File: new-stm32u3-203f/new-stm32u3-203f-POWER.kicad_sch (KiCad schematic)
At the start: 15 parts, among them U4 LD39050PU33R, U5 TLV62569DBVR

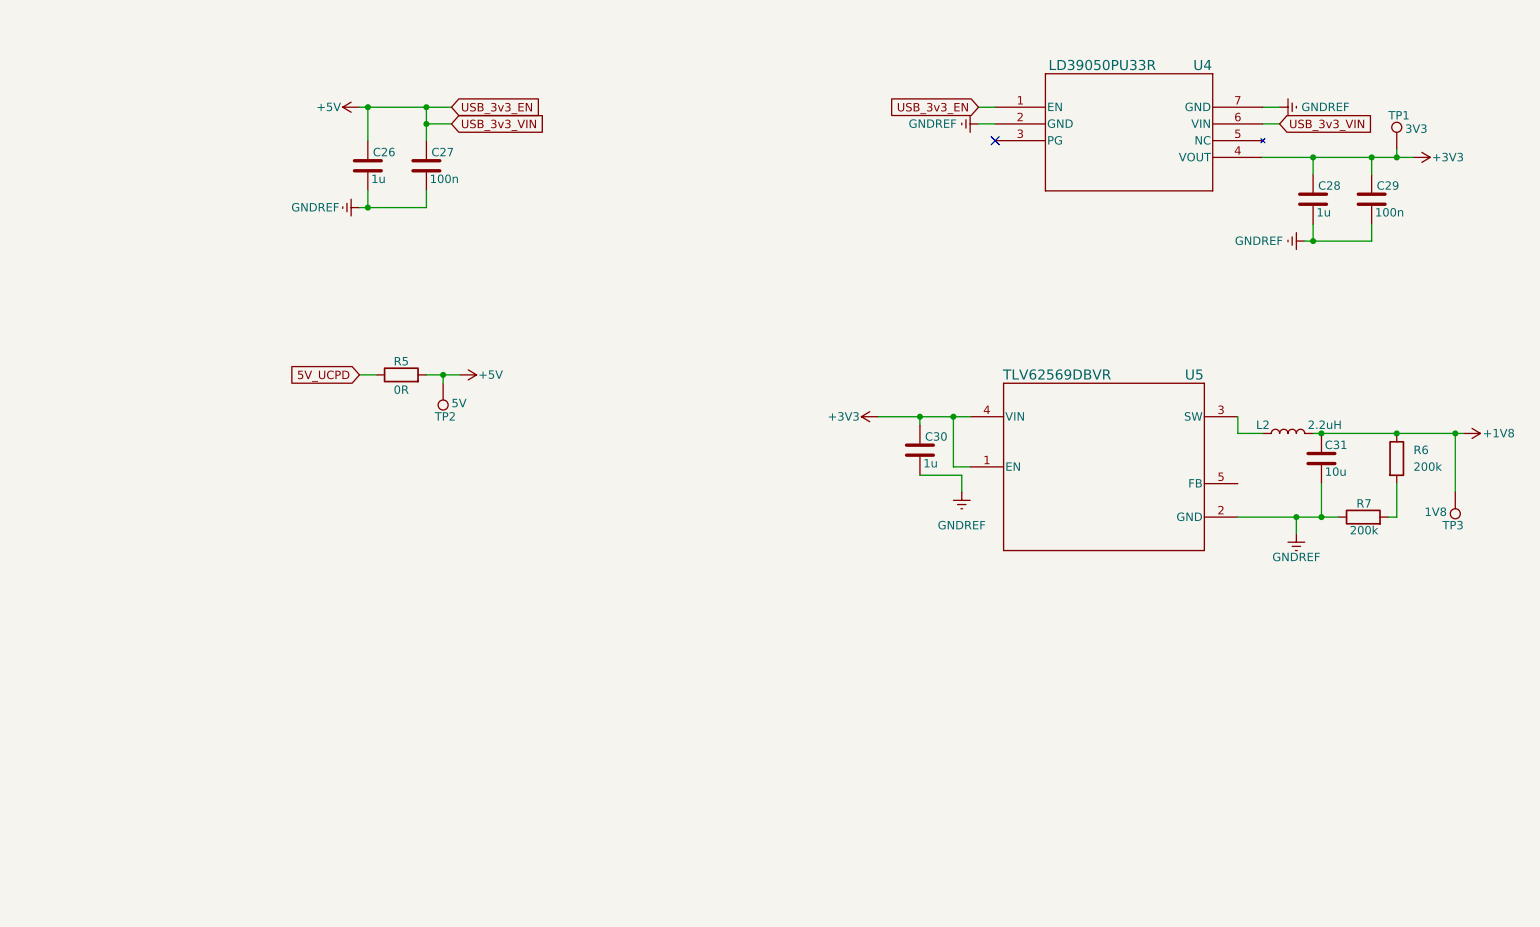
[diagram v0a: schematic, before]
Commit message: added battery charging circuit
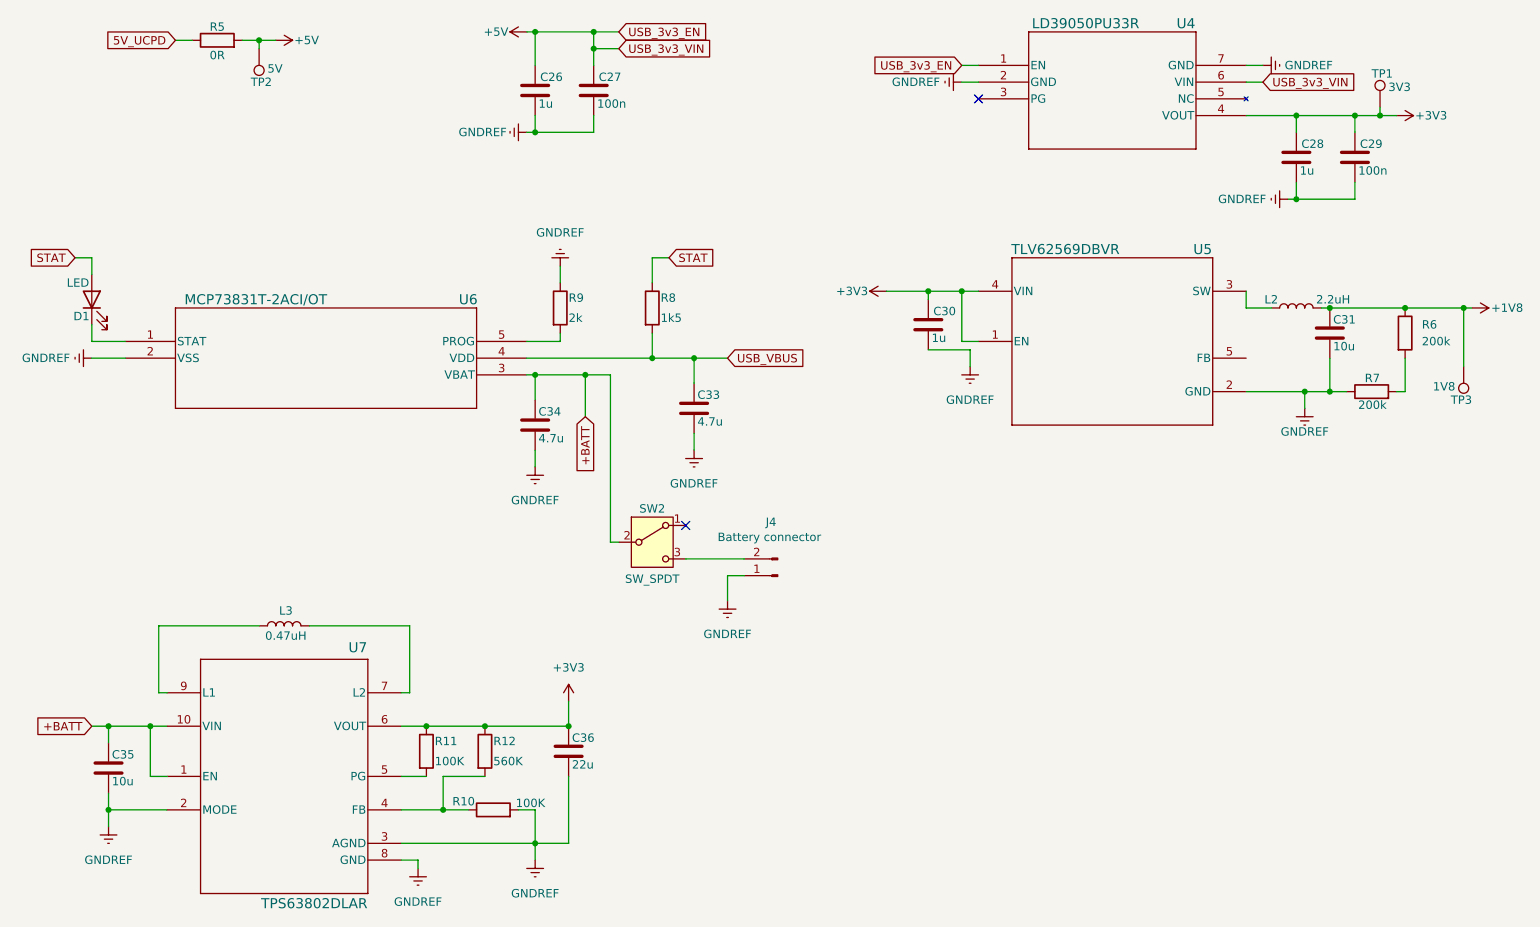
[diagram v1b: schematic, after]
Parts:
- added C33, C34: 4.7u, symbol Device:C
- added C35: 10u, symbol Device:C
- added C36: 22u, symbol Device:C
- added D1: LED, symbol Device:LED
- added J4: Battery connector, symbol Connector:Conn_01x02_Pin
- added L3: 0.47uH, symbol Device:L
- added R10, R11: 100K, symbol Device:R
- added R12: 560K, symbol Device:R
- added R8: 1k5, symbol Device:R
- added R9: 2k, symbol Device:R
- added SW2: SW_SPDT, symbol Switch:SW_SPDT
- added U6: MCP73831T-2ACI/OT, SOT-23-5_MC_MCH, symbol 2026-01-27_09-44-44:MCP73831T-2ACI_OT
- added U7: TPS63802DLAR, DLA0010A, symbol 2026-01-27_10-03-29:TPS63802DLAR
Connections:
- net +3V3: now also C36.2, R11.1, R12.1, U7.6 (VOUT)
- net GNDREF: now also C33.1, C34.1, C35.1, C36.1, J4.1 (Pin_1), R10.2, R9.1, U6.2 (VSS), U7.2 (MODE), U7.3 (AGND), U7.8 (GND)
- new net: D1.1 (K), U6.1 (STAT)
- new net: R9.2, U6.5 (PROG)
- new net: R10.1, R12.2, U7.4 (FB)
- new net: R11.2, U7.5 (PG)
- new net: L3.2, U7.7 (L2)
- new net: L3.1, U7.9 (L1)
- new net: J4.2 (Pin_2), SW2.3 (C)
- new net +BATT: C34.2, C35.2, SW2.2 (B), U6.3 (VBAT), U7.1 (EN), U7.10 (VIN)
- new net STAT: D1.2 (A), R8.1
- new net USB_VBUS: C33.2, R8.2, U6.4 (VDD)
- no-connect marks 1 -> 2
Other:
- moved on the sheet: C26, C27, C28, C29, C30, C31, L2, R5, R6, R7, TP1, TP2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

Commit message: finished the schematic, just need someone to review it :)
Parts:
- C30: value 1u -> 4.7u
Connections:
- net GNDREF: now also R7.2; no longer R7.1
- net at R6.2: now also R7.1, U5.5 (FB); no longer R7.2
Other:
- moved on the sheet: J4, SW2

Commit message: added reset button. asigned footprints.
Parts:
- C26, C27, C28, C29, C30, C31, C33, C34, C35, C36: footprint (none) -> Capacitor_SMD:C_0603_1608Metric
- D1: value LED -> LED_PWR_indicator; footprint (none) -> LED_SMD:LED_0603_1608Metric
- J4: footprint (none) -> Connector_PinHeader_2.54mm:PinHeader_1x04_P2.54mm_Vertical
- L2, L3: footprint (none) -> Inductor_SMD:L_0603_1608Metric
- R10, R11, R12, R5, R6, R7, R8, R9: footprint (none) -> Resistor_SMD:R_0603_1608Metric
- SW2: footprint (none) -> footprints_SPDT_slide:CL-SB-12B-01_NDC
- TP1, TP2, TP3: footprint (none) -> TestPoint:TestPoint_Pad_D1.0mm
- U4: footprint DFN6_3X3_STM -> Package_DFN_QFN:DFN-6-1EP_3x3mm_P0.95mm_EP1.7x2.6mm
- U5: footprint DBV0005A_N -> Package_TO_SOT_SMD:SOT-23-5
- U6: footprint SOT-23-5_MC_MCH -> Package_TO_SOT_SMD:SOT-23-5
- U7: footprint DLA0010A -> footprints:DLA0010A
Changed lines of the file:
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@@
 			)
 		)
-		(property "Footprint" ""
+		(property "Footprint" "Capacitor_SMD:C_0603_1608Metric"
 			(at 103.1748 36.83 0)
 			(effects
@@
 			)
 		)
-		(property "Footprint" ""
+		(property "Footprint" "Capacitor_SMD:C_0603_1608Metric"
 			(at 108.2548 137.16 0)
 			(effects
@@
 			)
 		)
-		(property "Footprint" ""
+		(property "Footprint" "Capacitor_SMD:C_0603_1608Metric"
 			(at 162.8648 72.39 0)
 			(effects
@@
 			)
 		)
-		(property "Footprint" ""
+		(property "Footprint" "Capacitor_SMD:C_0603_1608Metric"
 			(at 38.4048 139.7 0)
 			(effects
@@
 			)
 		)
-		(property "Footprint" ""
+		(property "Footprint" "Inductor_SMD:L_0603_1608Metric"
 			(at 219.71 73.66 0)
 			(effects
@@
 			)
 		)
-		(property "Footprint" ""
+		(property "Footprint" "Resistor_SMD:R_0603_1608Metric"
 			(at 234.442 77.47 90)
 			(effects
@@
 			)
 		)
-		(property "Footprint" "DFN6_3X3_STM"
+		(property "Footprint" "Package_DFN_QFN:DFN-6-1EP_3x3mm_P0.95mm_EP1.7x2.6mm"
 			(at 171.45 36.83 0)
 			(effects
@@
 			)
 		)
-		(property "Footprint" "SOT-23-5_MC_MCH"
+		(property "Footprint" "Package_TO_SOT_SMD:SOT-23-5"
 			(at 41.91 78.74 0)
 			(effects
@@
 			)
 		)
-		(property "Footprint" ""
+		(property "Footprint" "Resistor_SMD:R_0603_1608Metric"
 			(at 234.442 95.25 90)
 			(effects
@@
 			)
 		)
-		(property "Footprint" ""
+		(property "Footprint" "Capacitor_SMD:C_0603_1608Metric"
 			(at 112.0648 36.83 0)
 			(effects
@@
 			)
 		)
-		(property "Footprint" ""
+		(property "Footprint" "Resistor_SMD:R_0603_1608Metric"
 			(at 94.742 140.97 90)
 			(effects
@@
 			)
 		)
-		(property "Footprint" ""
+		(property "Footprint" "Capacitor_SMD:C_0603_1608Metric"
 			(at 227.6348 46.99 0)
 			(effects
@@
 			)
 		)
-		(property "Footprint" "DBV0005A_N"
+		(property "Footprint" "Package_TO_SOT_SMD:SOT-23-5"
 			(at 191.77 78.74 0)
 			(effects
@@
 			)
 		)
-		(property "Footprint" ""
+		(property "Footprint" "TestPoint:TestPoint_Pad_D1.0mm"
 			(at 240.03 82.55 0)
 			(effects
@@
 			)
 		)
-		(property "Footprint" ""
+		(property "Footprint" "TestPoint:TestPoint_Pad_D1.0mm"
 			(at 237.49 43.18 0)
 			(effects
@@
 			)
 		)
-		(property "Footprint" ""
+		(property "Footprint" "Capacitor_SMD:C_0603_1608Metric"
 			(at 218.7448 46.99 0)
 			(effects
@@
 			)
 		)
-		(property "Footprint" ""
+		(property "Footprint" "Resistor_SMD:R_0603_1608Metric"
 			(at 97.79 151.638 90)
 			(effects
@@
 			)
 		)
-		(property "Footprint" ""
+		(property "Footprint" "Resistor_SMD:R_0603_1608Metric"
 			(at 120.142 73.66 90)
 			(effects
@@
 			)
 		)
-		(property "Value" "LED"
-			(at 33.02 69.85 90)
+		(property "Value" "LED_PWR_indicator"
+			(at 27.94 70.104 90)
 			(effects
 				(font
@@
 			)
 		)
-		(property "Footprint" ""
+		(property "Footprint" "LED_SMD:LED_0603_1608Metric"
 			(at 36.83 72.39 0)
 			(effects
@@
 			)
 		)
-		(property "Footprint" ""
+		(property "Footprint" "Resistor_SMD:R_0603_1608Metric"
 			(at 55.88 34.798 90)
 			(effects
@@
 			)
 		)
-		(property "Footprint" "DLA0010A"
+		(property "Footprint" "footprints:DLA0010A"
 			(at 66.04 144.78 0)
 			(effects
@@
 			)
 		)
-		(property "Footprint" ""
+		(property "Footprint" "Resistor_SMD:R_0603_1608Metric"
 			(at 85.852 140.97 90)
 			(effects
@@
 			)
 		)
-		(property "Footprint" ""
+		(property "Footprint" "Capacitor_SMD:C_0603_1608Metric"
 			(at 223.8248 73.66 0)
 			(effects
@@
 			)
 		)
-		(property "Footprint" ""
+		(property "Footprint" "Inductor_SMD:L_0603_1608Metric"
 			(at 66.04 121.92 0)
 			(effects
@@
 			)
 		)
-		(property "Footprint" ""
+		(property "Footprint" "Connector_PinHeader_2.54mm:PinHeader_1x04_P2.54mm_Vertical"
 			(at 140.97 113.03 0)
 			(effects
@@
 			)
 		)
-		(property "Footprint" ""
+		(property "Footprint" "Capacitor_SMD:C_0603_1608Metric"
 			(at 127.3048 85.09 0)
 			(effects
@@
 			)
 		)
-		(property "Footprint" ""
+		(property "Footprint" "footprints_SPDT_slide:CL-SB-12B-01_NDC"
 			(at 121.92 107.95 0)
 			(effects
@@
 			)
 		)
-		(property "Footprint" ""
+		(property "Footprint" "Resistor_SMD:R_0603_1608Metric"
 			(at 106.172 73.66 90)
 			(effects
@@
 			)
 		)
-		(property "Footprint" ""
+		(property "Footprint" "TestPoint:TestPoint_Pad_D1.0mm"
 			(at 67.31 34.29 0)
 			(effects
@@
 			)
 		)
-		(property "Footprint" ""
+		(property "Footprint" "Capacitor_SMD:C_0603_1608Metric"
 			(at 103.1748 87.63 0)
 			(effects

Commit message: made some progress on the pcb
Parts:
- J4: footprint Connector_PinHeader_2.54mm:PinHeader_1x04_P2.54mm_Vertical -> Connector_PinHeader_2.54mm:PinHeader_1x02_P2.54mm_Vertical
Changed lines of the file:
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@@
 			)
 		)
-		(property "Footprint" "Connector_PinHeader_2.54mm:PinHeader_1x04_P2.54mm_Vertical"
+		(property "Footprint" "Connector_PinHeader_2.54mm:PinHeader_1x02_P2.54mm_Vertical"
 			(at 140.97 113.03 0)
 			(effects

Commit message: made some progress witht he layout.
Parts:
- removed R5: 0R, Resistor_SMD:R_0603_1608Metric, symbol Device:R
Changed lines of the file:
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@@
 	(wire
 		(pts
-			(xy 59.69 33.02) (xy 62.23 33.02)
-		)
-		(stroke
-			(width 0)
-			(type default)
-		)
-	)
-	(wire
-		(pts
 			(xy 163.83 71.12) (xy 163.83 72.39)
 		)
@@
 	(wire
 		(pts
-			(xy 49.53 33.02) (xy 52.07 33.02)
+			(xy 49.53 33.02) (xy 62.23 33.02)
 		)
 		(stroke
@@
 					(unit 1)
 				)
-			)
-		)
-	)
-	(symbol
-		(lib_id "Device:R")
-		(at 55.88 33.02 90)
-		(unit 1)
-		(exclude_from_sim no)
-		(in_bom yes)
-		(on_board yes)
-		(dnp no)
-		(property "Reference" "R5"
-			(at 55.88 30.988 90)
-			(effects
-				(font
-					(size 1.27 1.27)
-				)
-			)
-		)
-		(property "Value" "0R"
-			(at 55.88 35.306 90)
-			(effects
-				(font
-					(size 1.27 1.27)
-				)
-			)
-		)
-		(property "Footprint" "Resistor_SMD:R_0603_1608Metric"
-			(at 55.88 34.798 90)
-			(effects
-				(font
-					(size 1.27 1.27)
-				)
-				(hide yes)
-			)
-		)
-		(property "Datasheet" "~"
-			(at 55.88 33.02 0)
-			(effects
-				(font
-					(size 1.27 1.27)
-				)
-				(hide yes)
-			)
-		)
-		(property "Description" "Resistor"
-			(at 55.88 33.02 0)
-			(effects
-				(font
-					(size 1.27 1.27)
-				)
-				(hide yes)
-			)
-		)
-		(pin "1"
-		)
-		(pin "2"
-		)
-		(instances
-			(project "new-stm32u3-203f"
-				(path "/133609ce-1e1a-4c9a-bce3-37a0219dc965/fbdd0d38-3709-4a96-99fb-af9d998b7f91"
-					(reference "R5")
-					(unit 1)
-				)

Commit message: moved over to just using direct usb 2.0, made progress on pcb layout
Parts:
- added R3, R4: 202k, Resistor_SMD:R_0603_1608Metric, symbol Device:R
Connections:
- net USB_VBUS is gone; now on net +5V: C33.2, R8.2, U6.4 (VDD)
- net +BATT: now also R3.1
- net GNDREF: now also R4.1
- new net BATT_MON: R3.2, R4.2

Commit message: finished the layout of the pcb
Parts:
- removed SW2: SW_SPDT, footprints_SPDT_slide:CL-SB-12B-01_NDC, symbol Switch:SW_SPDT
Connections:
- net +BATT: now also J4.2 (Pin_2)
- no-connect marks 2 -> 1
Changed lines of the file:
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@@
 		(at 171.45 41.91)
 	)
-	(no_connect
-		(at 127 105.41)
-	)
 	(wire
 		(pts
@@
 	(wire
 		(pts
-			(xy 127 110.49) (xy 135.89 110.49)
-		)
-		(stroke
-			(width 0)
-			(type default)
-		)
-	)
-	(wire
-		(pts
 			(xy 166.37 115.57) (xy 162.56 115.57)
 		)
@@
 	(wire
 		(pts
-			(xy 115.57 107.95) (xy 115.57 83.82)
+			(xy 115.57 110.49) (xy 115.57 83.82)
 		)
 		(stroke
@@
 	(wire
 		(pts
-			(xy 115.57 107.95) (xy 116.84 107.95)
+			(xy 115.57 110.49) (xy 135.89 110.49)
 		)
 		(stroke
@@
 					(unit 1)
 				)
-			)
-		)
-	)
-	(symbol
-		(lib_id "Switch:SW_SPDT")
-		(at 121.92 107.95 0)
-		(unit 1)
-		(exclude_from_sim no)
-		(in_bom yes)
-		(on_board yes)
-		(dnp no)
-		(property "Reference" "SW2"
-			(at 121.92 102.87 0)
-			(effects
-				(font
-					(size 1.27 1.27)
-				)
-			)
-		)
-		(property "Value" "SW_SPDT"
-			(at 121.92 113.538 0)
-			(effects
-				(font
-					(size 1.27 1.27)
-				)
-			)
-		)
-		(property "Footprint" "footprints_SPDT_slide:CL-SB-12B-01_NDC"
-			(at 121.92 107.95 0)
-			(effects
-				(font
-					(size 1.27 1.27)
-				)
-				(hide yes)
-			)
-		)
-		(property "Datasheet" "~"
-			(at 121.92 115.57 0)
-			(effects
-				(font
-					(size 1.27 1.27)
-				)
-				(hide yes)
-			)
-		)
-		(property "Description" "Switch, single pole double throw"
-			(at 121.92 107.95 0)
-			(effects
-				(font
-					(size 1.27 1.27)
-				)
-				(hide yes)
-			)
-		)
-		(pin "1"
-		)
-		(pin "3"
-		)
-		(pin "2"
-		)
-		(instances
-			(project ""
-				(path "/133609ce-1e1a-4c9a-bce3-37a0219dc965/fbdd0d38-3709-4a96-99fb-af9d998b7f91"
-					(reference "SW2")
-					(unit 1)
-				)

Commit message: made some better progress routing
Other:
- moved on the sheet: C26
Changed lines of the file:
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@@
 	(symbol
 		(lib_id "Device:C")
-		(at 104.14 40.64 180)
+		(at 104.14 40.64 0)
+		(mirror x)
 		(unit 1)
 		(exclude_from_sim no)
@@
 		(dnp no)
 		(property "Reference" "C26"
-			(at 104.902 38.608 0)
+			(at 103.378 38.608 0)
 			(effects
 				(font
@@
 		)
 		(property "Value" "1u"
-			(at 104.648 42.672 0)
+			(at 103.632 42.672 0)
 			(effects
 				(font
@@
 		)
 		(property "Footprint" "Capacitor_SMD:C_0603_1608Metric"
-			(at 103.1748 36.83 0)
+			(at 105.1052 36.83 0)
 			(effects
 				(font
